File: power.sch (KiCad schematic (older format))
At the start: 18 parts, among them J18 XT60PW-F_Vertical, J19 XT90PW-M, Q6 BSS138DW, Q7 BSS138DW, U13 D36V50F5, U14 D36V28F3, U15 TLV75528PDBV, U16 CMX60D20, U17 TLV75518PDBV

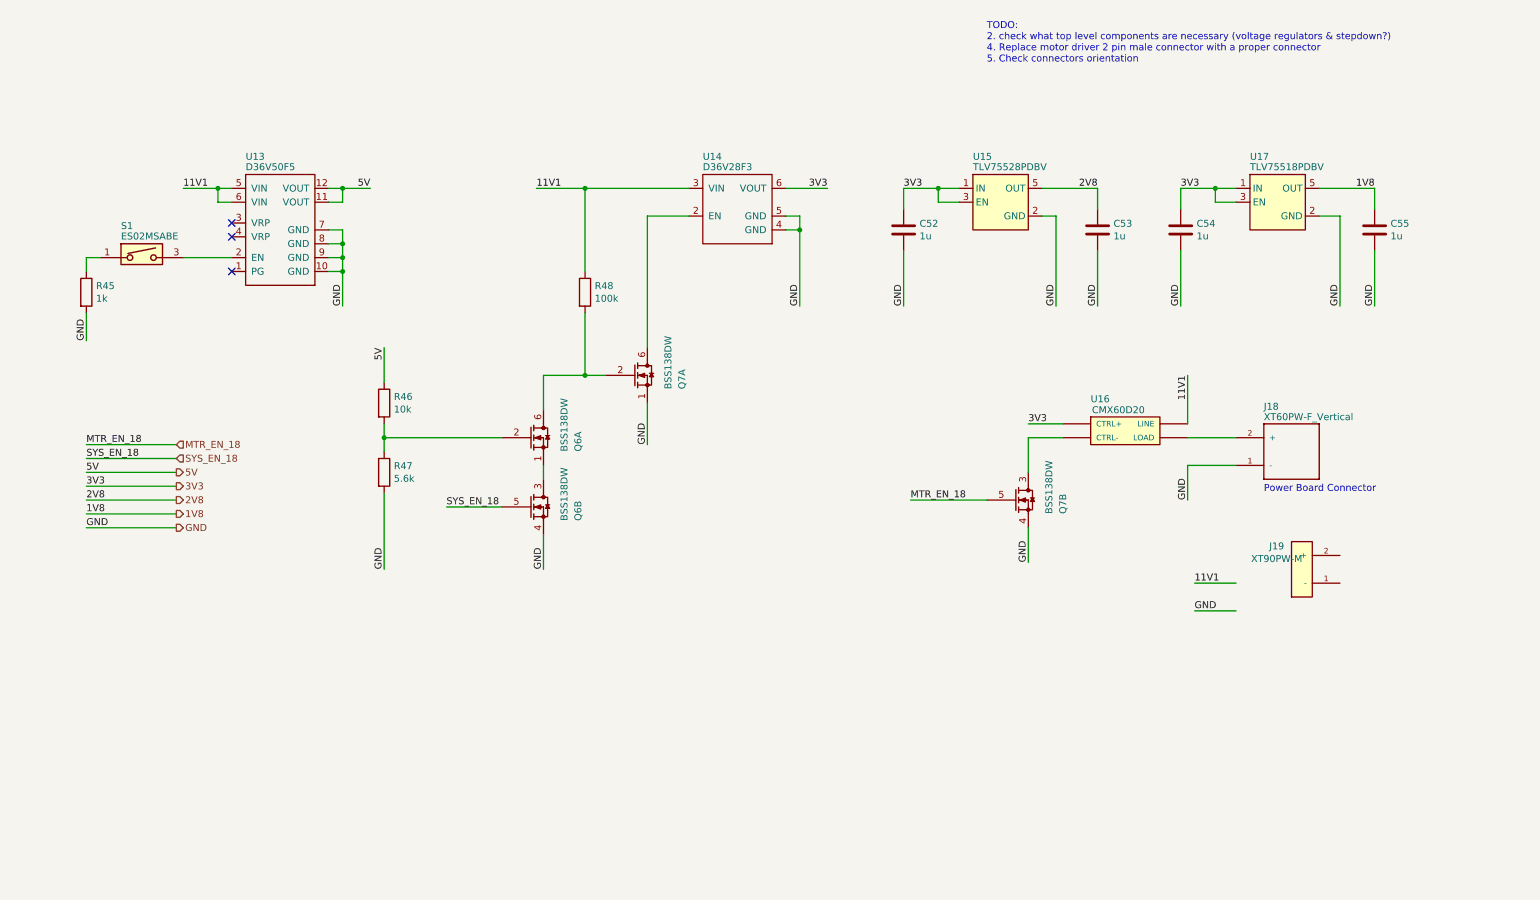
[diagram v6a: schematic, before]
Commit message: Add Xbee to schematics and PCB layout.
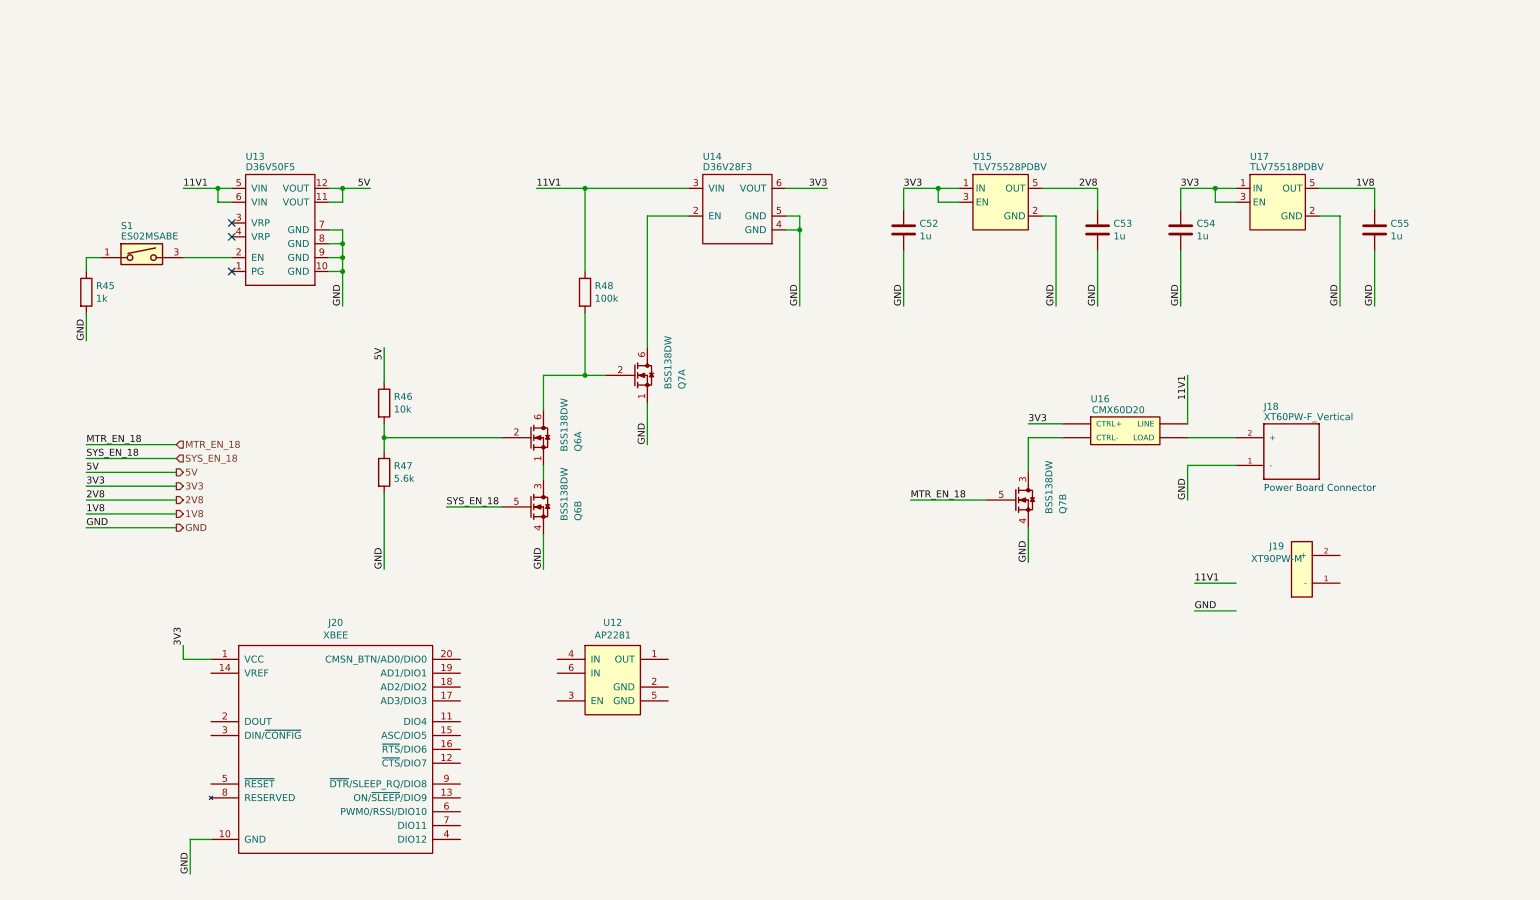
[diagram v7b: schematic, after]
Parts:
- added J20: XBEE, Drone:XBEE, symbol Drone:XBEE
- added U12: AP2281, Drone:AP2281, symbol Drone:AP2281
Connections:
- net 3V3: now also J20.1 (VCC)
- net GND: now also J20.10 (GND)
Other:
- note removed: "TODO: \n2. check what top level components are necessary (voltage regulators & stepdown?)\n4. Replace motor driver 2 pin male connector with a proper connector\n5. Check connectors orientation\n"
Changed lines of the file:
@@
 	1    0    0    -1
 $EndComp
-Text Notes 7600 950  0    50   ~ 0
-TODO: \n2. check what top level components are necessary (voltage regulators & stepdown?)\n4. Replace motor driver 2 pin male connector with a proper connector\n5. Check connectors orientation\n
 Text HLabel 1750 3800 2    50   Input ~ 0
 SYS_EN_18
@@
 Text Label 3250 4600 1    50   ~ 0
 GND
+$Comp
+L Drone:XBEE J20
+U 1 1 5E5DEFCB
+P 2200 5150
+F 0 "J20" H 2900 5315 50  0000 C CNN
+F 1 "XBEE" H 2900 5224 50  0000 C CNN
+F 2 "Drone:XBEE" H 2400 3600 50  0001 C CNN
+F 3 "https://www.sparkfun.com/pages/xbee_guide" H 2200 5150 50  0001 C CNN
+	1    2200 5150
+	1    0    0    -1
+$EndComp
+Text Label 1850 6800 1    50   ~ 0
+GND
+Wire Wire Line
+	1850 6800 1850 6550
+Wire Wire Line
+	1850 6550 2000 6550
+Text Label 1800 5150 1    50   ~ 0
+3V3
+Wire Wire Line
+	2000 5250 1800 5250
+Wire Wire Line
+	1800 5250 1800 5150
+$Comp
+L Drone:AP2281 U12
+U 1 1 5E6384D1
+P 4700 5150
+F 0 "U12" H 4900 5315 50  0000 C CNN
+F 1 "AP2281" H 4900 5224 50  0000 C CNN
+F 2 "Drone:AP2281" H 4950 4600 50  0001 C CNN
+F 3 "https://www.diodes.com/assets/Datasheets/AP2281.pdf" H 5750 4700 50  0001 C CNN
+	1    4700 5150
+	1    0    0    -1
+$EndComp
 $EndSCHEMATC

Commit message: Work in progess on integrating the Xbee into the design.
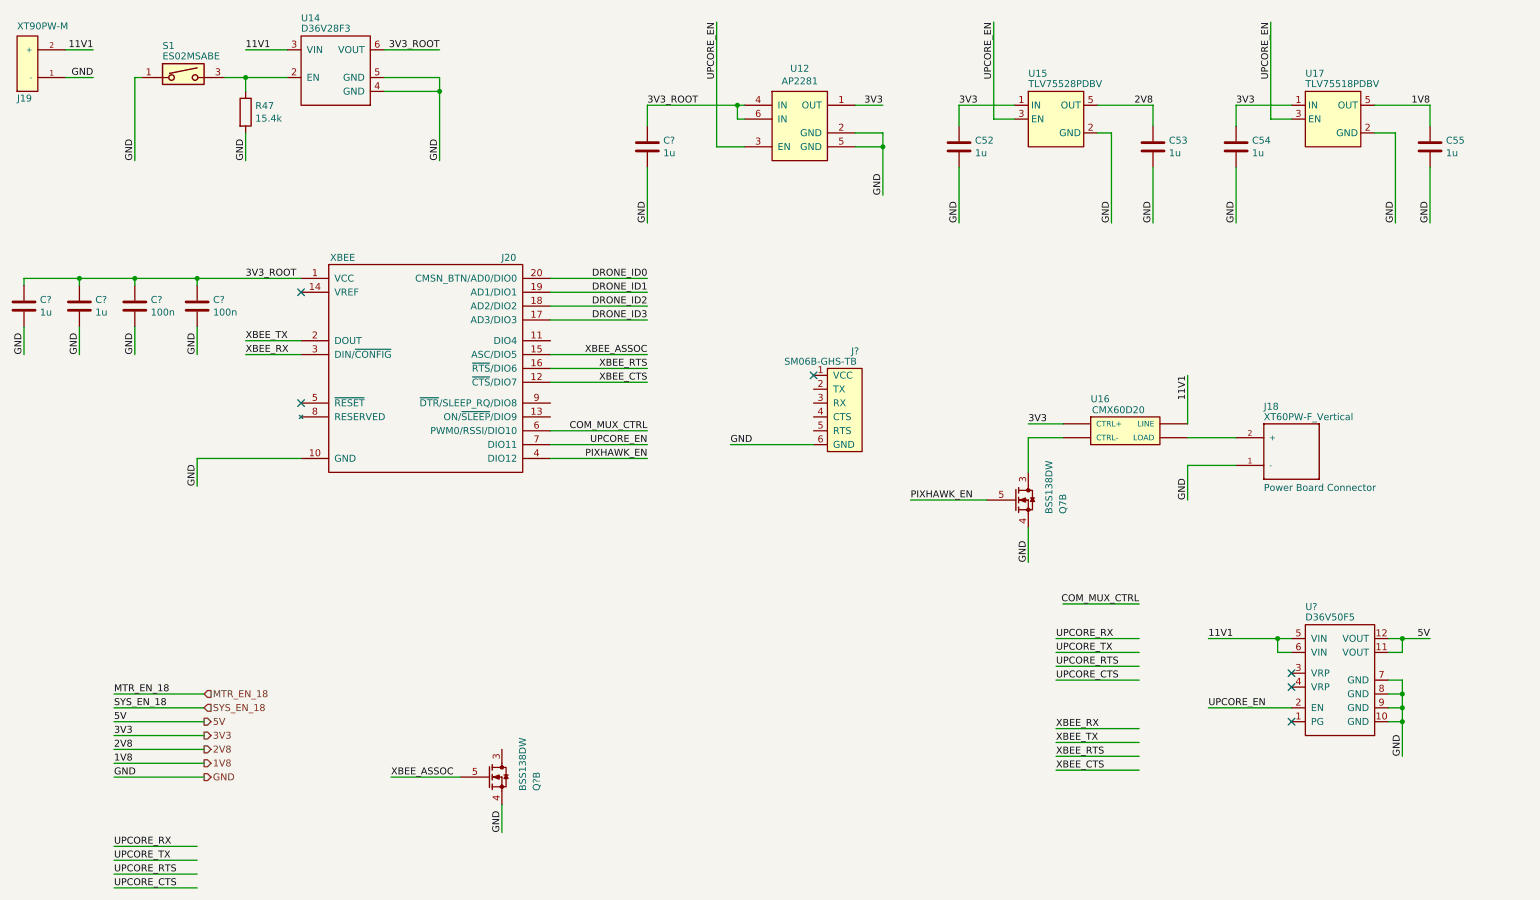
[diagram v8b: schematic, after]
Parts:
- removed Q6: BSS138DW, Package_TO_SOT_SMD:SOT-363_SC-70-6, symbol Drone:BSS138DW
- removed unit 1 of Q7
- removed R45: 1k, Drone:R0805, symbol Drone:RES
- removed R46: 10k, Drone:R0805, symbol Drone:RES
- removed R48: 100k, Drone:R0805, symbol Drone:RES
- removed U13: D36V50F5, Drone:D36V50F5_S, symbol Drone:D36V50F5
- added C? (x3): 1u, Drone:C0805, symbol Drone:CAP
- added C? (x2): 100n, Drone:C0805, symbol Drone:CAP
- added J?: SM06B-GHS-TB, Drone:JST_GH_SM06B-GHS-TB, symbol Drone:SM06B-GHS-TB
- added Q?: BSS138DW, Package_TO_SOT_SMD:SOT-363_SC-70-6, symbol Drone:BSS138DW
- added U?: D36V50F5, Drone:D36V50F5_S, symbol Drone:D36V50F5
- R47: value 5.6k -> 15.4k
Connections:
- net labels added: 3V3_ROOT, COM_MUX_CTRL, DRONE_ID0, DRONE_ID1, DRONE_ID2, DRONE_ID3, PIXHAWK_EN, UPCORE_CTS, UPCORE_EN, UPCORE_RTS, UPCORE_RX, UPCORE_TX, XBEE_ASSOC, XBEE_CTS, XBEE_RTS, XBEE_RX, XBEE_TX
- wire segments 87 -> 122
- no-connect marks 3 -> 6
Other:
- moved on the sheet: C52, C53, C54, C55, J19, J20, R47, S1, U12, U14, U15, U17
